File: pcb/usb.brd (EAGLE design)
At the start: 26.2 x 26.2 mm, 26 parts, among them J1 JSTPH, Q1 DMG3415U, Q2 mmbt2222, Q3 mmbt2222, U1 MIC5225-3.3v, U2 CH340C, U3 MCP73831T-2ACI/OT

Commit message: Add manufacturer part numbers to USB board
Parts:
- Q1: value DMG3415U -> ZXMP6A13FTA

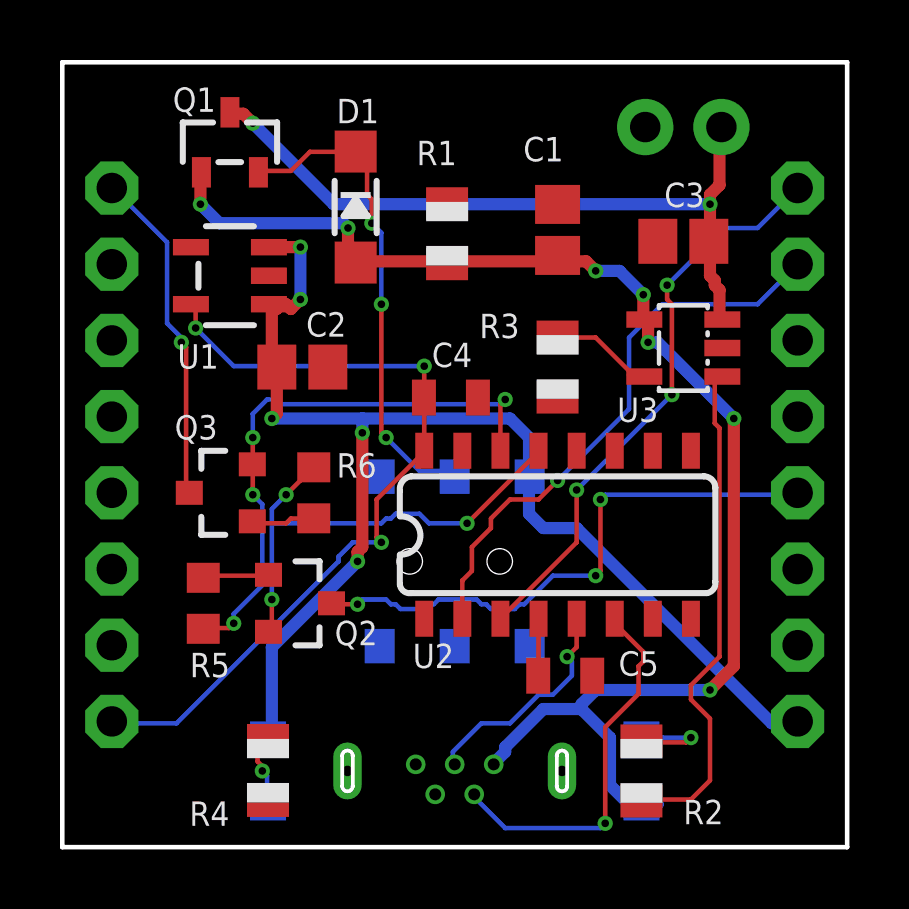
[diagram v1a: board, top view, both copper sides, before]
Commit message: Mark a trace as power in the USB board
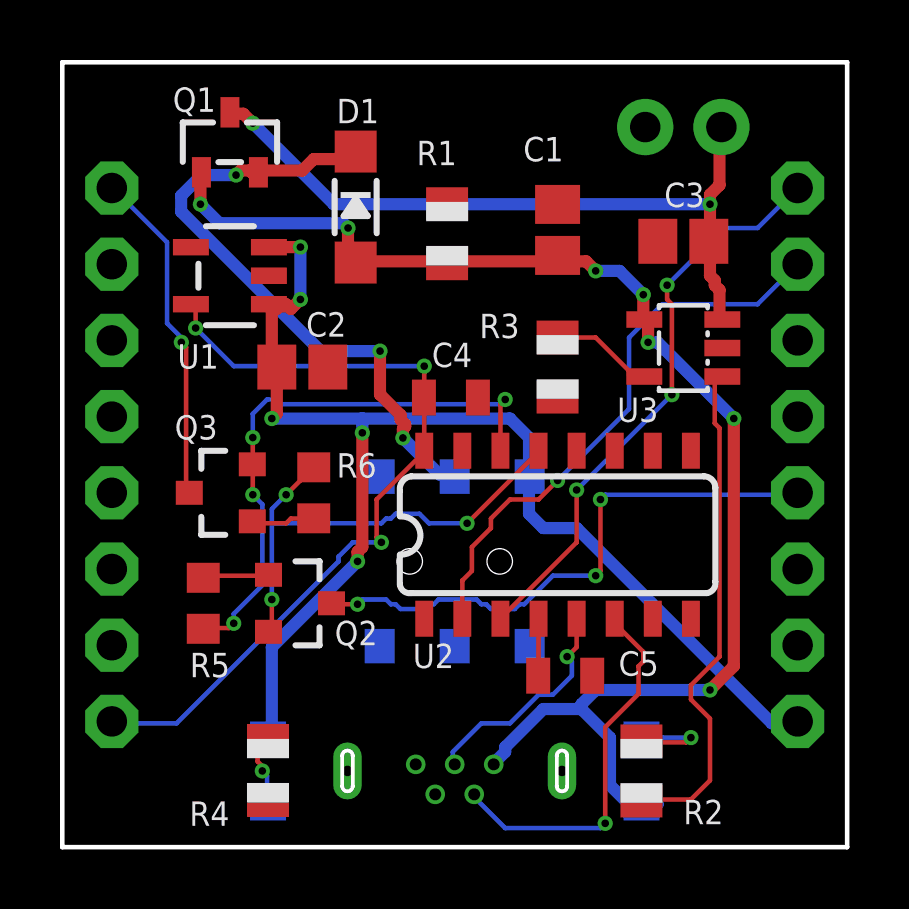
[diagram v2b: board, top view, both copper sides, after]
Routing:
- net N$7: track 16.6 -> 21.1 mm
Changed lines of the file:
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@@
 <layer number="14" name="Route14" color="1" fill="6" visible="no" active="no"/>
 <layer number="15" name="Route15" color="4" fill="6" visible="no" active="no"/>
-<layer number="16" name="Bottom" color="1" fill="1" visible="no" active="yes"/>
+<layer number="16" name="Bottom" color="1" fill="1" visible="yes" active="yes"/>
 <layer number="17" name="Pads" color="2" fill="1" visible="yes" active="yes"/>
 <layer number="18" name="Vias" color="2" fill="1" visible="yes" active="yes"/>
 <layer number="19" name="Unrouted" color="6" fill="1" visible="yes" active="yes"/>
 <layer number="20" name="Dimension" color="15" fill="1" visible="yes" active="yes"/>
-<layer number="21" name="tPlace" color="14" fill="1" visible="yes" active="yes"/>
-<layer number="22" name="bPlace" color="5" fill="1" visible="no" active="yes"/>
-<layer number="23" name="tOrigins" color="14" fill="1" visible="yes" active="yes"/>
-<layer number="24" name="bOrigins" color="13" fill="1" visible="no" active="yes"/>
-<layer number="25" name="tNames" color="7" fill="1" visible="yes" active="yes"/>
-<layer number="26" name="bNames" color="7" fill="1" visible="no" active="yes"/>
+<layer number="21" name="tPlace" color="14" fill="1" visible="no" active="yes"/>
+<layer number="22" name="bPlace" color="5" fill="1" visible="yes" active="yes"/>
+<layer number="23" name="tOrigins" color="14" fill="1" visible="no" active="yes"/>
+<layer number="24" name="bOrigins" color="13" fill="1" visible="yes" active="yes"/>
+<layer number="25" name="tNames" color="7" fill="1" visible="no" active="yes"/>
+<layer number="26" name="bNames" color="7" fill="1" visible="yes" active="yes"/>
 <layer number="27" name="tValues" color="7" fill="1" visible="no" active="yes"/>
 <layer number="28" name="bValues" color="7" fill="1" visible="no" active="yes"/>
@@
 <layer number="37" name="tTest" color="7" fill="1" visible="no" active="yes"/>
 <layer number="38" name="bTest" color="7" fill="1" visible="no" active="yes"/>
-<layer number="39" name="tKeepout" color="4" fill="11" visible="yes" active="yes"/>
-<layer number="40" name="bKeepout" color="1" fill="11" visible="no" active="yes"/>
-<layer number="41" name="tRestrict" color="4" fill="10" visible="yes" active="yes"/>
-<layer number="42" name="bRestrict" color="1" fill="10" visible="no" active="yes"/>
+<layer number="39" name="tKeepout" color="4" fill="11" visible="no" active="yes"/>
+<layer number="40" name="bKeepout" color="1" fill="11" visible="yes" active="yes"/>
+<layer number="41" name="tRestrict" color="4" fill="10" visible="no" active="yes"/>
+<layer number="42" name="bRestrict" color="1" fill="10" visible="yes" active="yes"/>
 <layer number="43" name="vRestrict" color="2" fill="10" visible="no" active="yes"/>
 <layer number="44" name="Drills" color="7" fill="1" visible="no" active="yes"/>
@@
 <layer number="49" name="Reference" color="7" fill="1" visible="no" active="yes"/>
 <layer number="50" name="dxf" color="7" fill="1" visible="no" active="yes"/>
-<layer number="51" name="tDocu" color="7" fill="1" visible="yes" active="yes"/>
-<layer number="52" name="bDocu" color="7" fill="1" visible="no" active="yes"/>
+<layer number="51" name="tDocu" color="7" fill="1" visible="no" active="yes"/>
+<layer number="52" name="bDocu" color="7" fill="1" visible="yes" active="yes"/>
 <layer number="53" name="tGND_GNDA" color="7" fill="9" visible="no" active="no"/>
 <layer number="54" name="bGND_GNDA" color="1" fill="9" visible="no" active="no"/>
@@
 <contactref element="JP2" pad="3"/>
 </signal>
-<signal name="N$7">
+<signal name="N$7" class="1">
 <contactref element="D1" pad="C"/>
 <contactref element="Q1" pad="2"/>
 <contactref element="S1" pad="2"/>
-<wire x1="7.62" y1="22.5425" x2="6.6675" y2="22.5425" width="0.1524" layer="1"/>
-<wire x1="8.255" y1="23.1775" x2="7.62" y2="22.5425" width="0.1524" layer="1"/>
-<wire x1="9.68375" y1="23.1775" x2="8.255" y2="23.1775" width="0.1524" layer="1"/>
-<wire x1="6.6675" y1="22.5425" x2="6.538" y2="22.495" width="0.1524" layer="1"/>
-<wire x1="9.68375" y1="23.1775" x2="9.779" y2="23.186" width="0.1524" layer="1"/>
-<wire x1="13.0175" y1="12.54125" x2="13.0175" y2="12.3825" width="0.1524" layer="16"/>
-<wire x1="11.90625" y1="12.54125" x2="13.0175" y2="12.54125" width="0.1524" layer="16"/>
-<wire x1="10.795" y1="13.6525" x2="11.90625" y2="12.54125" width="0.1524" layer="16"/>
-<wire x1="10.63625" y1="13.81125" x2="10.795" y2="13.6525" width="0.1524" layer="1"/>
-<wire x1="10.63625" y1="18.0975" x2="10.63625" y2="13.81125" width="0.1524" layer="1"/>
-<wire x1="10.63625" y1="20.47875" x2="10.63625" y2="18.0975" width="0.1524" layer="16"/>
-<wire x1="10.31875" y1="20.79625" x2="10.63625" y2="20.47875" width="0.1524" layer="16"/>
-<wire x1="10.31875" y1="21.59" x2="10.31875" y2="20.79625" width="0.1524" layer="1"/>
-<wire x1="10.16" y1="21.74875" x2="10.31875" y2="21.59" width="0.1524" layer="1"/>
-<wire x1="10.16" y1="23.1775" x2="10.16" y2="21.74875" width="0.1524" layer="1"/>
-<wire x1="9.8425" y1="23.1775" x2="10.16" y2="23.1775" width="0.1524" layer="1"/>
-<wire x1="13.0175" y1="12.3825" x2="13.081" y2="12.35" width="0.1524" layer="16"/>
-<wire x1="9.8425" y1="23.1775" x2="9.779" y2="23.186" width="0.1524" layer="1"/>
-<via x="10.795" y="13.6525" extent="1-16" drill="0.254"/>
-<via x="10.63625" y="18.0975" extent="1-16" drill="0.254"/>
-<via x="10.31875" y="20.79625" extent="1-16" drill="0.254"/>
+<wire x1="8.001" y1="22.5552" x2="6.5532" y2="22.5552" width="0.4064" layer="1"/>
+<wire x1="8.382" y1="22.9362" x2="8.001" y2="22.5552" width="0.4064" layer="1"/>
+<wire x1="9.525" y1="22.9362" x2="8.382" y2="22.9362" width="0.4064" layer="1"/>
+<wire x1="9.7536" y1="23.1648" x2="9.525" y2="22.9362" width="0.4064" layer="1"/>
+<wire x1="6.5532" y1="22.5552" x2="6.538" y2="22.495" width="0.4064" layer="1"/>
+<wire x1="9.7536" y1="23.1648" x2="9.779" y2="23.186" width="0.4064" layer="1"/>
+<wire x1="12.573" y1="12.4206" x2="13.0302" y2="12.4206" width="0.4064" layer="16"/>
+<wire x1="11.3538" y1="13.6398" x2="12.573" y2="12.4206" width="0.4064" layer="16"/>
+<wire x1="11.3538" y1="13.9446" x2="11.3538" y2="13.6398" width="0.4064" layer="1"/>
+<wire x1="11.43" y1="14.0208" x2="11.3538" y2="13.9446" width="0.4064" layer="1"/>
+<wire x1="11.43" y1="14.097" x2="11.43" y2="14.0208" width="0.4064" layer="1"/>
+<wire x1="11.2776" y1="14.2494" x2="11.43" y2="14.097" width="0.4064" layer="1"/>
+<wire x1="11.2776" y1="14.4018" x2="11.2776" y2="14.2494" width="0.4064" layer="1"/>
+<wire x1="10.5918" y1="15.0876" x2="11.2776" y2="14.4018" width="0.4064" layer="1"/>
+<wire x1="10.5918" y1="16.5354" x2="10.5918" y2="15.0876" width="0.4064" layer="1"/>
+<wire x1="8.6106" y1="16.5354" x2="10.5918" y2="16.5354" width="0.4064" layer="16"/>
+<wire x1="3.9624" y1="21.1836" x2="8.6106" y2="16.5354" width="0.4064" layer="16"/>
+<wire x1="3.9624" y1="21.717" x2="3.9624" y2="21.1836" width="0.4064" layer="16"/>
+<wire x1="4.6482" y1="22.4028" x2="3.9624" y2="21.717" width="0.4064" layer="16"/>
+<wire x1="5.7912" y1="22.4028" x2="4.6482" y2="22.4028" width="0.4064" layer="16"/>
+<wire x1="5.9436" y1="22.5552" x2="5.7912" y2="22.4028" width="0.4064" layer="1"/>
+<wire x1="6.2484" y1="22.5552" x2="5.9436" y2="22.5552" width="0.4064" layer="1"/>
+<wire x1="6.3246" y1="22.479" x2="6.2484" y2="22.5552" width="0.4064" layer="1"/>
+<wire x1="13.0302" y1="12.4206" x2="13.081" y2="12.35" width="0.4064" layer="16"/>
+<wire x1="6.3246" y1="22.479" x2="6.538" y2="22.495" width="0.4064" layer="1"/>
+<via x="11.3538" y="13.6398" extent="1-16" drill="0.254"/>
+<via x="10.5918" y="16.5354" extent="1-16" drill="0.254"/>
+<via x="5.7912" y="22.4028" extent="1-16" drill="0.254"/>
 </signal>
 <signal name="VIN" class="1">
